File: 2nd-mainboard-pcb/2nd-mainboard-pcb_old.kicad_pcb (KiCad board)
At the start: 2 copper layers, 99 x 99 mm, 132 parts, among them J1 PJ-082BH, J10 Servo Motor BL Touch, J11 T3, J12 Steckverbinder_Male_Fans, J13 Steckverbinder_Female_Leistung, J14 FAN3, J15 Steckverbinder_Female_Motoren, J16 ISP, J18 Quartz, J19 T2, J2 Fan_12/5V_Regelung, J20 T2, J21 T2, J22 T3, J23 Conn_01x04_Socket, J24 Steckverbinder_Male_Leistung, J3 Fan_12/5V_Regelung, J4 FAN0, J5 FAN1, J6 FAN2, J7 Stepper Motor, J8 Servo Motor SM, J9 Microstepping, P1 USB_C_Receptacle_USB2.0_14P, U1 SQJ409EP-T1_GE3, U10 ATmega328PB-A, U12 MPU-6050, U2 SZ1SMB5927BT3G, U3 TPS56837HRPAR, U4 TPS565208, U5 FT232RL, U6 PTS647SM38SMTR2LFS, U7 TPM16050-S6TR, U8 RJK0456DPB-00-J5, U9 RJK0456DPB-00-J5, Y1 ECS-160-18-4X-CKM

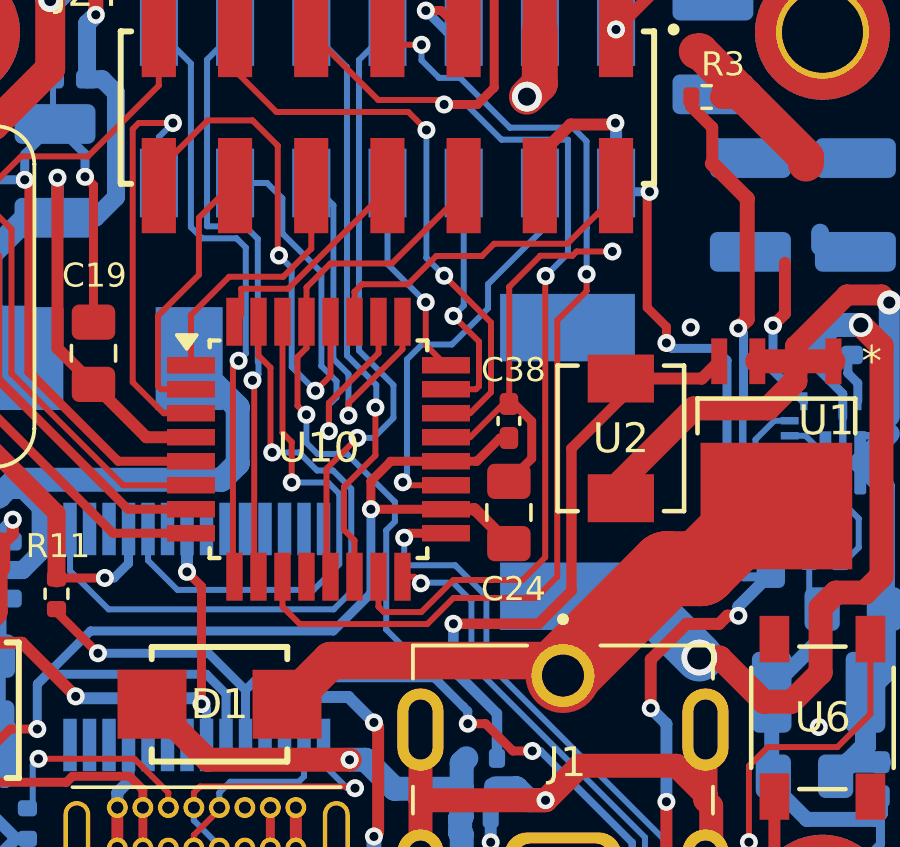
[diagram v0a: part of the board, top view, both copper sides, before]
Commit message: finished pcb design on main segment
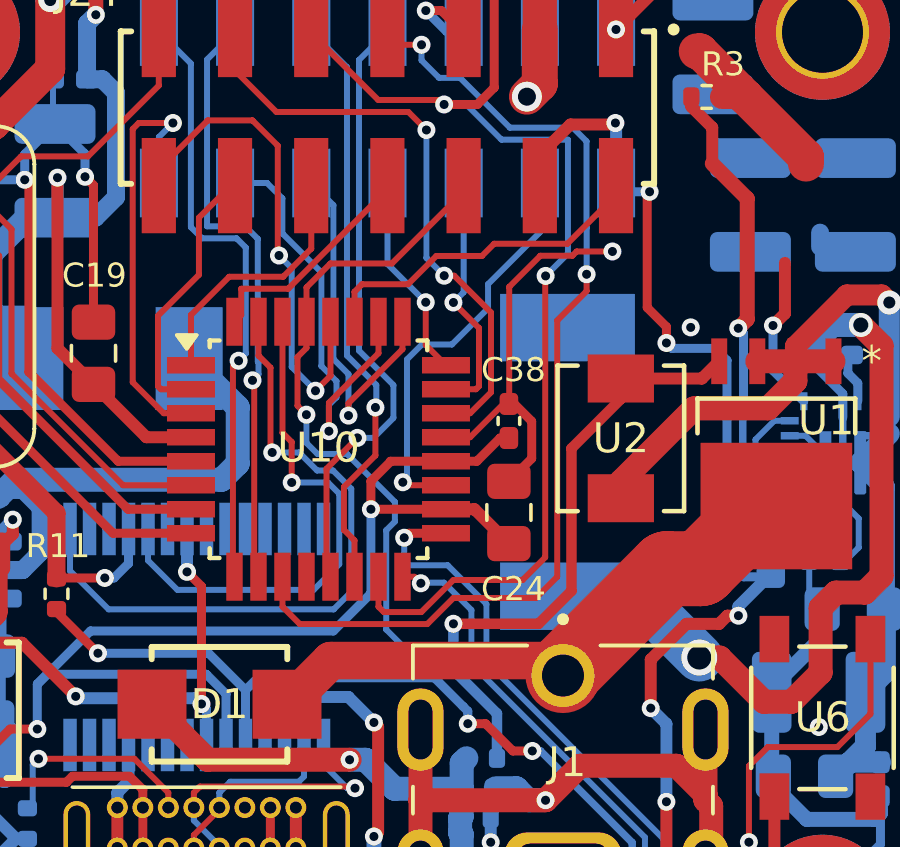
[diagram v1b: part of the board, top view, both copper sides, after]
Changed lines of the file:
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@@
 	)
 	(segment
+		(start 123.2025 124.5425)
+		(end 123.2025 122.6025)
+		(width 0.2)
+		(layer "F.Cu")
+		(net 3)
+	)
+	(segment
 		(start 67.049549 96.273624)
 		(end 67.298849 96.522924)
@@
 	)
 	(segment
-		(start 123.2025 123.052494)
-		(end 122.35 122.199994)
-		(width 0.2)
-		(layer "F.Cu")
-		(net 3)
-	)
-	(segment
-		(start 123.2025 124.5425)
-		(end 123.2025 123.052494)
+		(start 123.2025 122.6025)
+		(end 122.35 121.75)
 		(width 0.2)
 		(layer "F.Cu")
@@
 	)
 	(segment
-		(start 122.1025 124.6425)
-		(end 123.1025 124.6425)
-		(width 0.2)
+		(start 68.52 92.215424)
+		(end 67.668849 92.215424)
+		(width 0.4)
 		(layer "F.Cu")
 		(net 3)
 	)
 	(segment
-		(start 68.52 92.215424)
-		(end 67.668849 92.215424)
-		(width 0.4)
+		(start 122.1025 124.6425)
+		(end 123.1025 124.6425)
+		(width 0.2)
 		(layer "F.Cu")
 		(net 3)
@@
 	)
 	(via
-		(at 122.35 122.199994)
+		(at 122.35 121.75)
 		(size 0.6)
 		(drill 0.3)
@@
 	)
 	(segment
+		(start 122.6925 117.7675)
+		(end 122.6925 121.4075)
+		(width 0.2)
+		(layer "B.Cu")
+		(net 3)
+	)
+	(segment
 		(start 74.5 63)
 		(end 74.5 60.8)
@@
 	)
 	(segment
-		(start 122.6925 121.857494)
-		(end 122.35 122.199994)
-		(width 0.2)
-		(layer "B.Cu")
-		(net 3)
-	)
-	(segment
 		(start 77.85 64.75)
 		(end 76.65 63.55)
@@
 	)
 	(segment
-		(start 122.6925 117.7675)
-		(end 122.6925 121.857494)
+		(start 122.6925 121.4075)
+		(end 122.35 121.75)
 		(width 0.2)
 		(layer "B.Cu")
@@
 	)
 	(segment
-		(start 122.95 131.7)
-		(end 122.95 133.794538)
+		(start 122.04 131.09)
+		(end 122.95 132)
 		(width 0.2)
 		(layer "B.Cu")
@@
 	)
 	(segment
-		(start 129.160202 142.66)
-		(end 130.142702 142.66)
+		(start 128.734487 139.579025)
+		(end 128.734487 142.234285)
 		(width 0.2)
 		(layer "B.Cu")
@@
 	)
 	(segment
-		(start 122.34 131.09)
-		(end 122.95 131.7)
+		(start 121.28385 131.09)
+		(end 122.04 131.09)
 		(width 0.2)
 		(layer "B.Cu")
@@
 	)
 	(segment
-		(start 121.26385 131.11)
-		(end 121.28385 131.09)
+		(start 122.95 133.794538)
+		(end 128.734487 139.579025)
 		(width 0.2)
 		(layer "B.Cu")
@@
 	)
 	(segment
-		(start 128.734487 139.579025)
-		(end 128.734487 142.234285)
+		(start 129.160202 142.66)
+		(end 130.142702 142.66)
 		(width 0.2)
 		(layer "B.Cu")
@@
 	)
 	(segment
-		(start 121.28385 131.09)
-		(end 122.34 131.09)
+		(start 128.734487 142.234285)
+		(end 129.160202 142.66)
 		(width 0.2)
 		(layer "B.Cu")
@@
 	)
 	(segment
-		(start 128.734487 142.234285)
-		(end 129.160202 142.66)
+		(start 122.95 132)
+		(end 122.95 133.794538)
 		(width 0.2)
 		(layer "B.Cu")
@@
 	)
 	(segment
-		(start 122.95 133.794538)
-		(end 128.734487 139.579025)
+		(start 121.26385 131.11)
+		(end 121.28385 131.09)
 		(width 0.2)
 		(layer "B.Cu")
@@
 	)
 	(segment
-		(start 120.87 130.51)
-		(end 122.41 130.51)
+		(start 122.16 130.51)
+		(end 123.45 131.8)
 		(width 0.2)
 		(layer "B.Cu")
@@
 	)
 	(segment
-		(start 120.709 130.349)
-		(end 120.87 130.51)
+		(start 120.709 129.59251)
+		(end 120.709 130.349)
 		(width 0.2)
 		(layer "B.Cu")
@@
 	)
 	(segment
-		(start 120.709 129.59251)
-		(end 120.709 130.349)
+		(start 123.45 131.8)
+		(end 123.45 133.728852)
 		(width 0.2)
 		(layer "B.Cu")
@@
 	)
 	(segment
-		(start 122.41 130.51)
-		(end 123.45 131.55)
+		(start 123.45 133.728852)
+		(end 129.35 139.628852)
 		(width 0.2)
 		(layer "B.Cu")
@@
 	)
 	(segment
-		(start 123.45 131.55)
-		(end 123.45 133.728852)
+		(start 120.709 130.349)
+		(end 120.87 130.51)
 		(width 0.2)
 		(layer "B.Cu")
@@
 	)
 	(segment
-		(start 123.45 133.728852)
-		(end 129.35 139.628852)
+		(start 120.87 130.51)
+		(end 122.16 130.51)
 		(width 0.2)
 		(layer "B.Cu")
@@
 	)
 	(segment
+		(start 122.376739 120.8575)
+		(end 122.0425 120.8575)
+		(width 0.2)
+		(layer "F.Cu")
+		(net 102)
+	)
+	(segment
 		(start 89.9375 122.0375)
 		(end 89.9375 136.85)
@@
 	)
 	(segment
-		(start 123.6025 122.4175)
-		(end 122.0425 120.8575)
+		(start 123.6025 122.083261)
+		(end 122.376739 120.8575)
 		(width 0.2)
 		(layer "F.Cu")
@@
 	)
 	(segment
-		(start 122.1025 125.4425)
-		(end 122.9075 125.4425)
-		(width 0.2)
+		(start 83.92 116.02)
+		(end 89.9375 122.0375)
+		(width 0.3)
 		(layer "F.Cu")
 		(net 102)
 	)
 	(segment
-		(start 83.92 116.02)
-		(end 89.9375 122.0375)
-		(width 0.3)
+		(start 123.6025 124.7475)
+		(end 123.6025 122.083261)
+		(width 0.2)
 		(layer "F.Cu")
 		(net 102)
@@
 	)
 	(segment
-		(start 122.9075 125.4425)
-		(end 123.6025 124.7475)
+		(start 121.45 116)
+		(end 120.85 115.4)
 		(width 0.2)
 		(layer "F.Cu")
@@
 	)
 	(segment
-		(start 121.45 116)
-		(end 120.85 115.4)
+		(start 122.1025 125.4425)
+		(end 122.9075 125.4425)
 		(width 0.2)
 		(layer "F.Cu")
@@
 	)
 	(segment
-		(start 123.6025 124.7475)
-		(end 123.6025 122.4175)
+		(start 122.9075 125.4425)
+		(end 123.6025 124.7475)
 		(width 0.2)
 		(layer "F.Cu")
